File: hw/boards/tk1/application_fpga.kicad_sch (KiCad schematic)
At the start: 38 parts

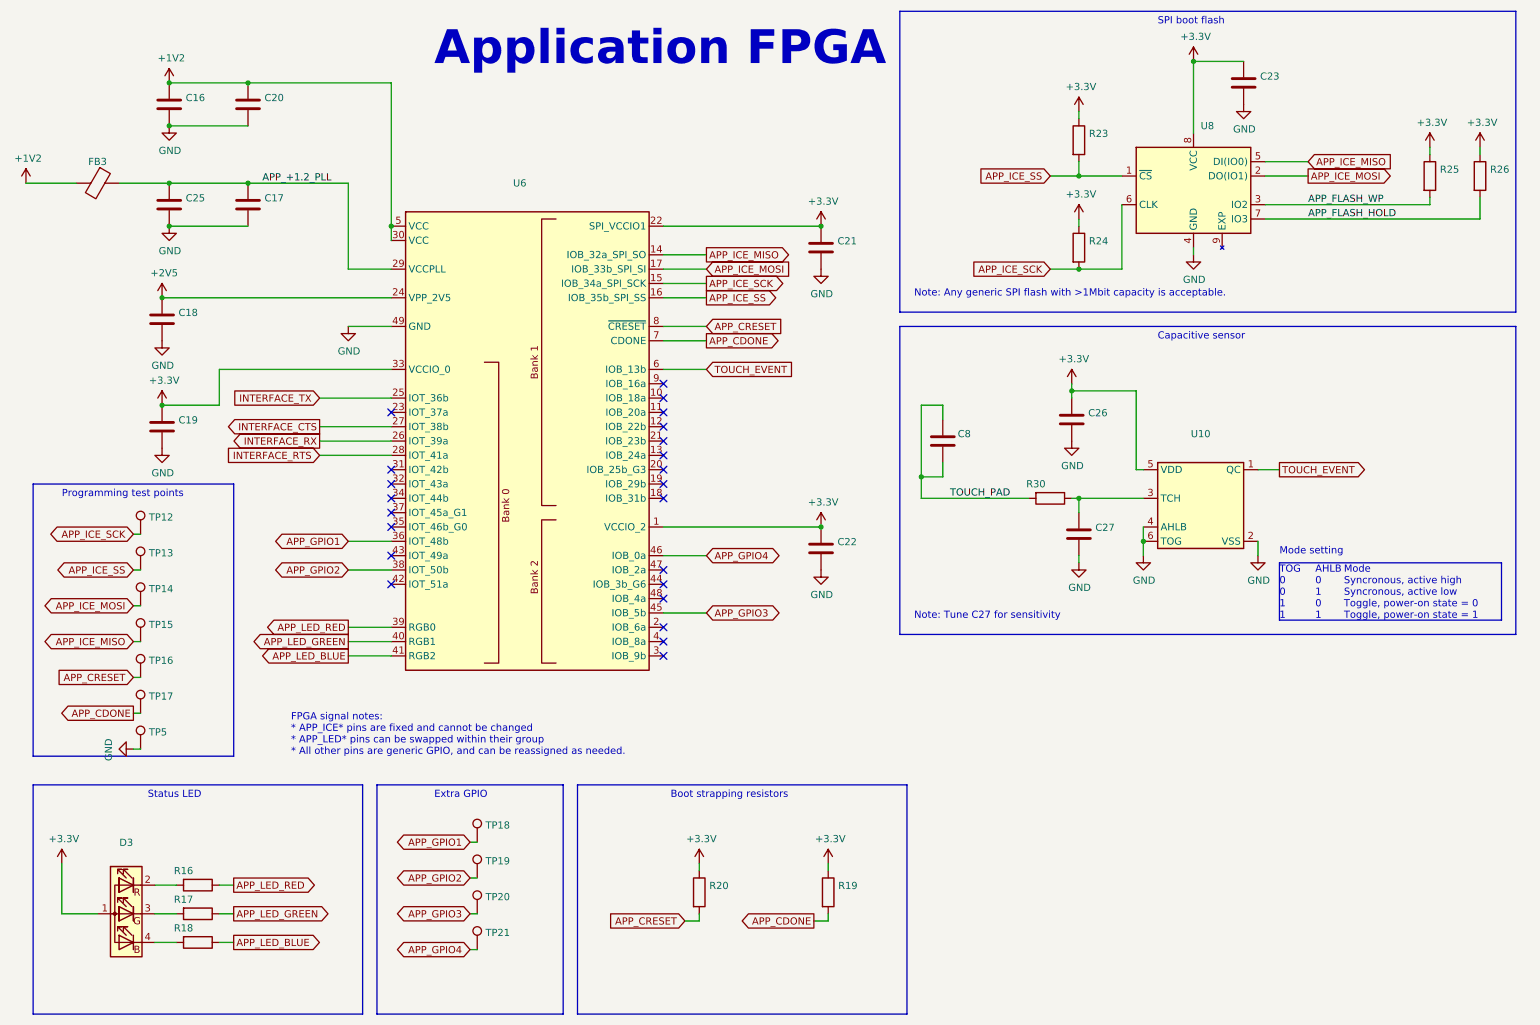
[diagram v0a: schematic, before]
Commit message: TK-1 and TP-1 PCBs (#52)
* Add kicad library for flat programming clip

* Add descriptions to part symbols

* Add extended values, manufacturer/distributor info to components in mta1

* Add new board entry for TK1

* Add TP1 programmer design

* Update MTA1-USB-V1 release files to match production

* Change SPI flash memory type to XT25F08BDFIGT-S
* Change touch sensor feedback cap to 1uF
* Add manufacturer, manufacturer part number, distributor, distributor part number

* Update component values for TK1 PCB

* Use specific part # for C8
* Change flash back to Winbond part, for easier sourcing
* Change C1 to 1pF

* Fixes for production programmer PCB

* Swap GND and 5V on J3
* Replace graphic logo with text
* Rename part to 'TP-1'

* TK-1 release

* Add dimensions for PCB
* Add layer stackup for PCB
* Change PCB component origin to match expanded board
* Change schematic title to 'TK-1', update release date

* mta1-usb-v1-programmer: Add corrected part numbers for OSFC production

* Q1, Q2, F1 part subsititutions
* add mfr/supplier info for all parts

* PCB library: add parts

* Rectangular footprint for TK-1 test pads
* BOM generation script used for TK-1 and TP-1 releases

* TP-1 release

* Schematic: Add manufacturer, supplier information for all parts
* Schematic: Update name and release date
* PCB: Add PCB fabrication information
* PCB: Correct pinouts on silkscreen

* PCB library: add 'screw' and 'foot' symbols

* Screw is a schematic-only part, for including mechanical screws in the
  BOM
* Foot is for self-adhesive rubber mounting feet that can be stuck to
  the bottom of a PCB

* TP-1 release: Add screws, feet to the BOM

* Pico library: Add footprint for RPi Pico w/solder paste

* TP-1 RevA release updates:

* Add fiducials in 3 corners (1mm exposed copper ring w/2mm soldermask opening)
* Add solder paste openings to Raspberry Pi Pico pads

* TK-1: RevA.1 release

* Add two fiducials to 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
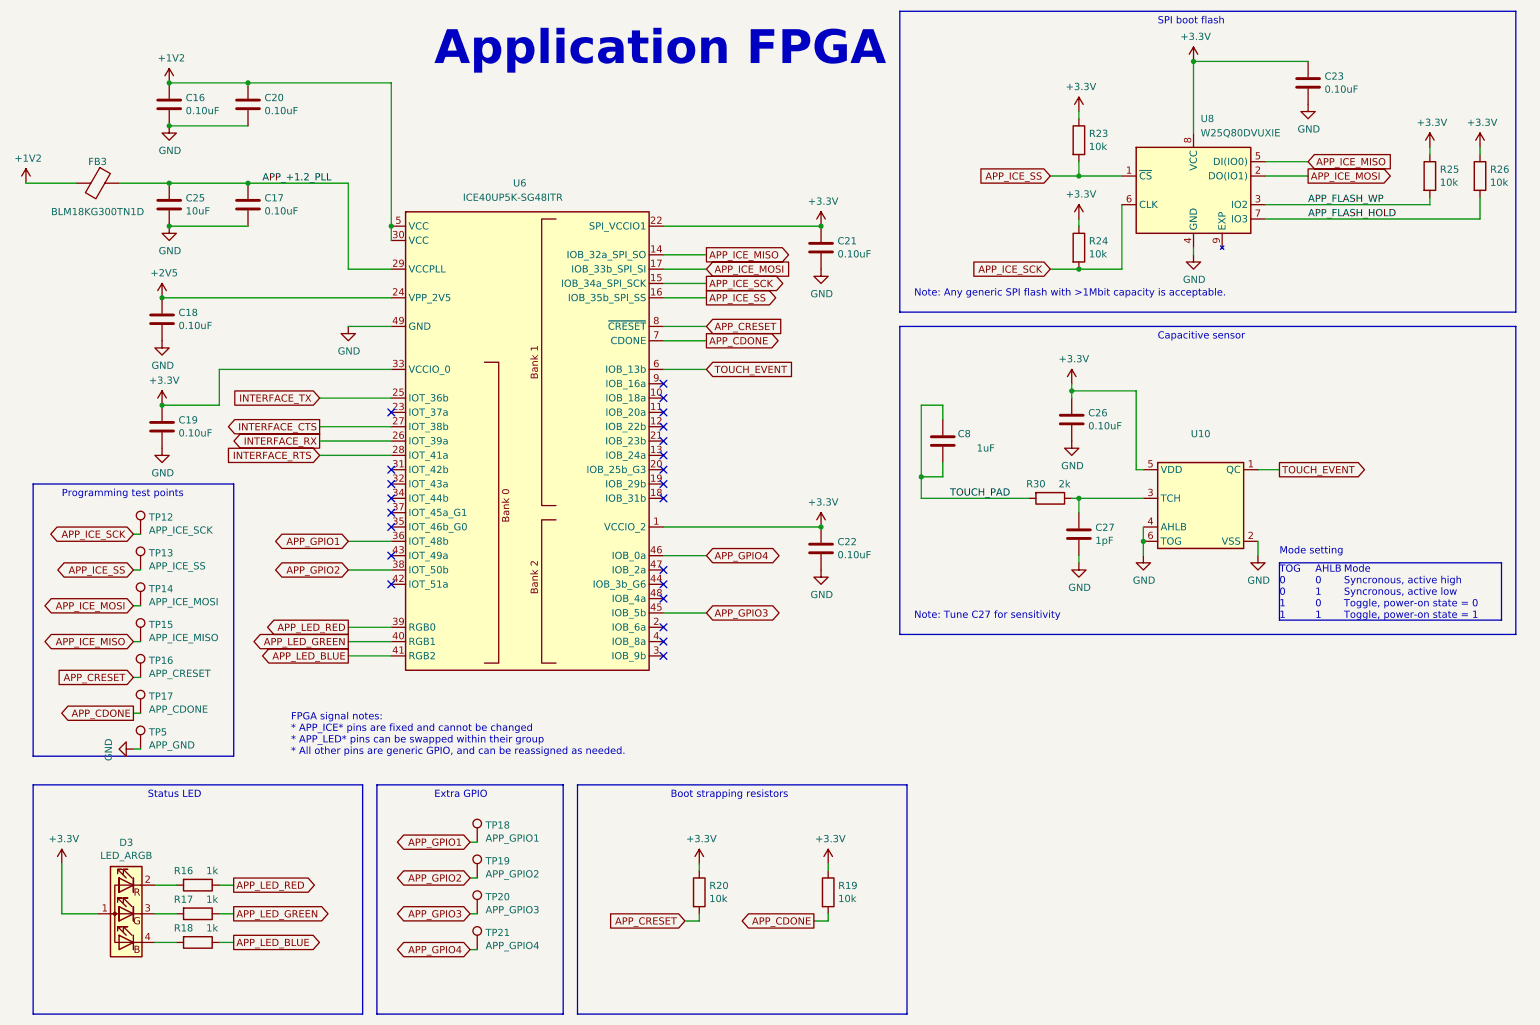
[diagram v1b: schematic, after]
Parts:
- C16, C17, C18, C19, C20, C21, C22, C23, C26: value (none) -> 0.10uF; footprint (none) -> mta1:CAPC1005X06L
- C25: value (none) -> 10uF; footprint (none) -> mta1:CAPC1608X09L
- C27: value (none) -> 1pF; footprint (none) -> mta1:CAPC1005X06L
- C8: value (none) -> 1uF; footprint (none) -> Capacitor_SMD:C_1206_3216Metric; Extended Value 16V,X5R,10% -> 50V,X7R,10%,1.6mm thickness; Manufacturer Fenghua -> TDK Corporation; Manufacturer Part Number 1206X106K160NT -> C3216X7R1H105K160AE; Supplier LCSC -> Digikey; Supplier Part Number C105478 -> 445-8904-2-ND
- D3: value (none) -> LED_ARGB; footprint (none) -> mta1:0402rgb-1010
- FB3: value (none) -> BLM18KG300TN1D; footprint (none) -> mta1:Ferritbead_0603_1608Metric
- R16, R17, R18: value (none) -> 1k; footprint (none) -> mta1:ERJ2G(0402)_L
- R19, R20, R23, R24, R25, R26: value (none) -> 10k; footprint (none) -> mta1:ERJ2G(0402)_L
- R30: value (none) -> 2k; footprint (none) -> mta1:ERJ2G(0402)_L
- TP12: value (none) -> APP_ICE_SCK; footprint (none) -> mta1:TestPoint_Pad_D1.0mm
- TP13: value (none) -> APP_ICE_SS; footprint (none) -> mta1:TestPoint_Pad_D1.0mm
- TP14: value (none) -> APP_ICE_MOSI; footprint (none) -> mta1:TestPoint_Pad_D1.0mm
- TP15: value (none) -> APP_ICE_MISO; footprint (none) -> mta1:TestPoint_Pad_D1.0mm
- TP16: value (none) -> APP_CRESET; footprint (none) -> mta1:TestPoint_Pad_D1.0mm
- TP17: value (none) -> APP_CDONE; footprint (none) -> mta1:TestPoint_Pad_D1.0mm
- TP18: value (none) -> APP_GPIO1; footprint (none) -> mta1:TestPoint_Pad_D1.0mm
- TP19: value (none) -> APP_GPIO2; footprint (none) -> mta1:TestPoint_Pad_D1.0mm
- TP20: value (none) -> APP_GPIO3; footprint (none) -> mta1:TestPoint_Pad_D1.0mm
- TP21: value (none) -> APP_GPIO4; footprint (none) -> mta1:TestPoint_Pad_D1.0mm
- TP5: value (none) -> APP_GND; footprint (none) -> mta1:TestPoint_Pad_D1.0mm
- U6: value (none) -> ICE40UP5K-SG48ITR; footprint (none) -> Package_DFN_QFN:QFN-48-1EP_7x7mm_P0.5mm_EP5.6x5.6mm
- U8: value (none) -> W25Q80DVUXIE; footprint (none) -> mta1:W25Q80DVUXIE; Manufacturer XTX -> Winbond Electronics; Manufacturer Part Number XT25F08BDFIGT-S -> W25Q80DVUXIE; Supplier LCSC -> Digikey; Supplier Part Number C558860 -> W25Q80DVUXIETR-ND
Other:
- moved on the sheet: C23
